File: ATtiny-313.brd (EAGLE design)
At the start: 27.6 x 64.1 mm, 14 parts

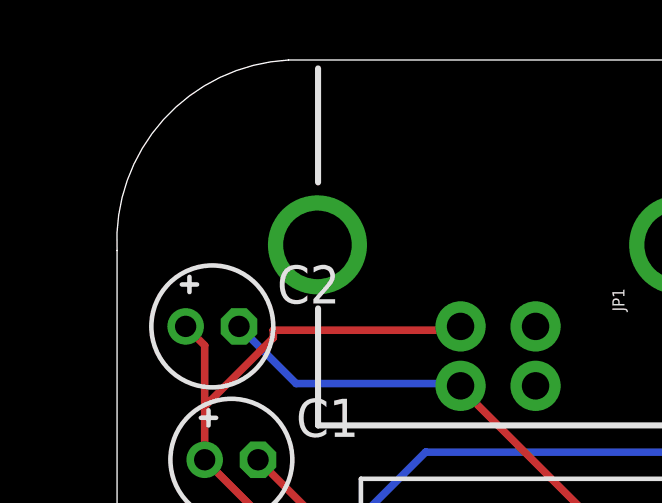
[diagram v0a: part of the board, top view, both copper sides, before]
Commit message: added link and OSHW logo
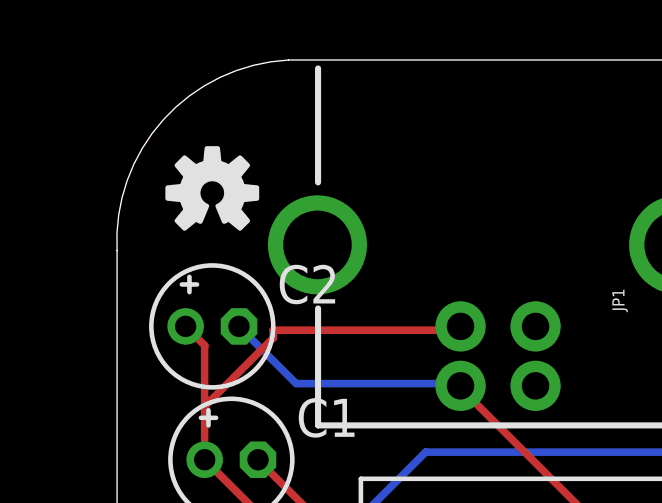
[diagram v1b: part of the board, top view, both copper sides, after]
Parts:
- added U$3: (no value), SparkFun-Aesthetics:OSHW-LOGO-S
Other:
- board text added: "http://github.com/jwhitehorn/ATtiny-313"
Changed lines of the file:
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@@
 <grid distance="0.025" unitdist="inch" unit="inch" style="lines" multiple="1" display="yes" altdistance="0.025" altunitdist="inch" altunit="inch"/>
 <layers>
-<layer number="1" name="Top" color="4" fill="1" visible="yes" active="yes"/>
+<layer number="1" name="Top" color="4" fill="1" visible="no" active="yes"/>
 <layer number="16" name="Bottom" color="1" fill="1" visible="yes" active="yes"/>
 <layer number="17" name="Pads" color="2" fill="1" visible="yes" active="yes"/>
@@
 <text x="32.385" y="36.83" size="1.016" layer="21">PD5</text>
 <text x="32.385" y="34.29" size="1.016" layer="21">GND</text>
+<text x="34.925" y="49.53" size="1.27" layer="22" rot="MR270">http://github.com/jwhitehorn/ATtiny-313</text>
 </plain>
 <attributes>
@@
 <element name="JP4" library="pinhead" package="1X01" value="" x="37.465" y="60.325"/>
 <element name="U$2" library="SparkFun-Electromechanical" package="STAND-OFF" value="" x="36.195" y="67.945"/>
+<element name="U$3" library="SparkFun-Aesthetics" package="OSHW-LOGO-S" value="" x="15.24" y="67.31"/>
 </elements>
 <signals>

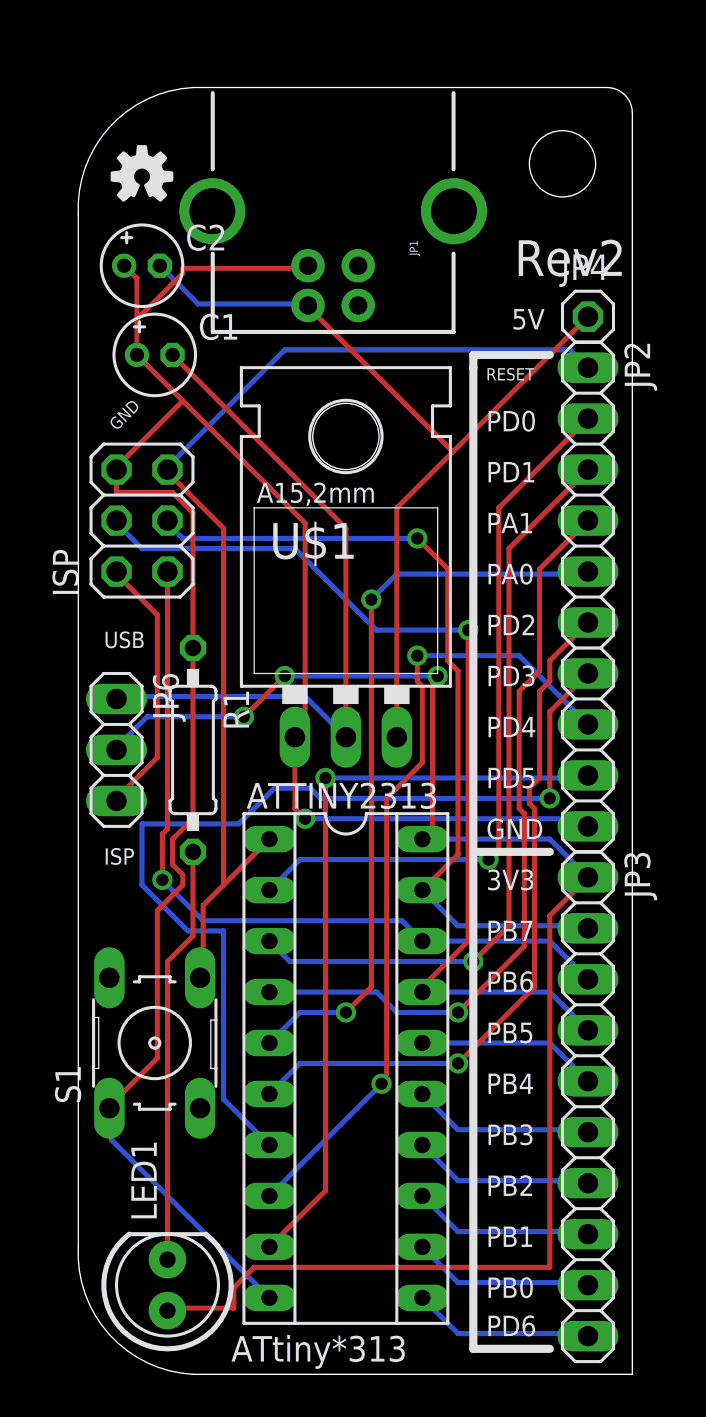
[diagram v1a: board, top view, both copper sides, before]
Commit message: use SMD to tighten up design
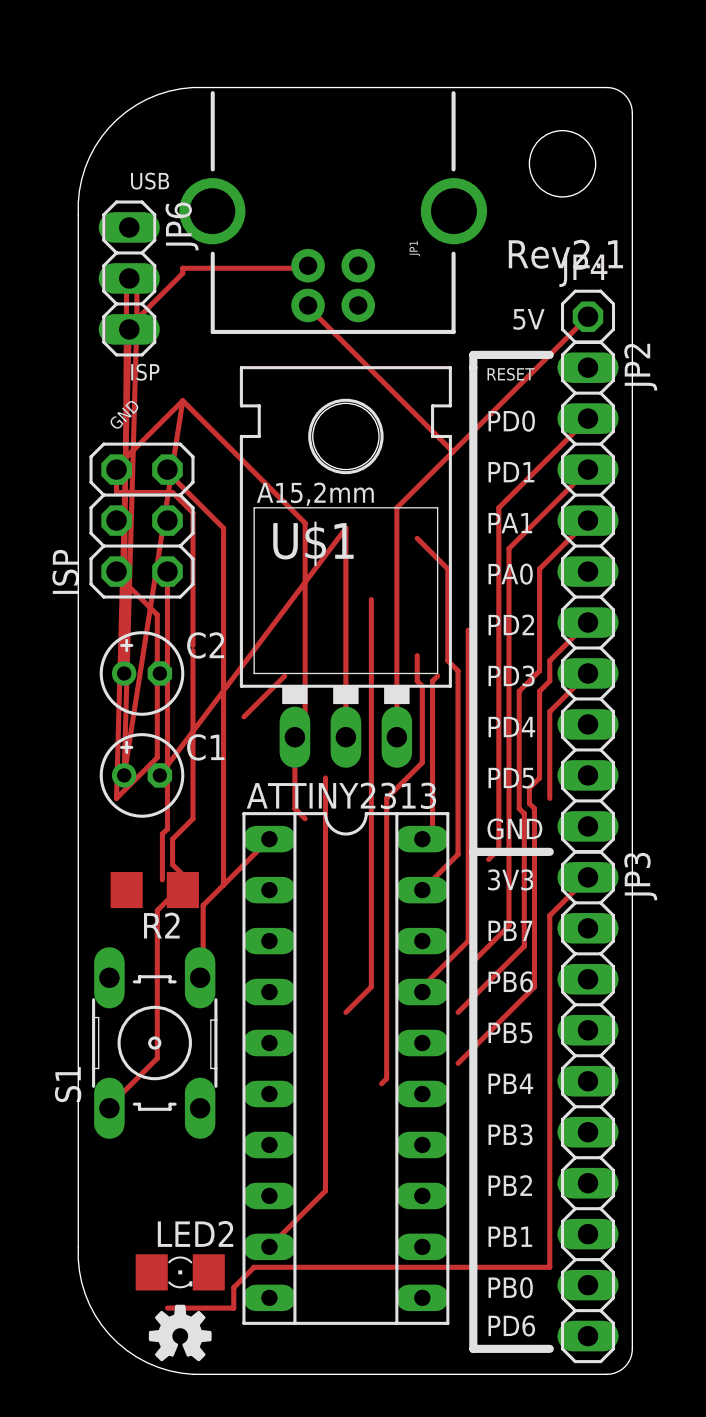
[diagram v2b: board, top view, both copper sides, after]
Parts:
- removed LED1: (no value), SparkFun-LED:LED5MM
- removed R1: 68, resistor:0207/10
- added LED2: (no value), led:1206
- added R2: 680, resistor:R3216
- moved U$3 57.8 mm to (17.1, 9.53)
- moved JP6 23.5 mm to (14.6, 62.2)
- moved C1 21.0 mm to (15.2, 37.5)
- moved C2 20.3 mm to (15.2, 42.5)
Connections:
- net N$2: now also LED2.A; no longer LED1.A
- net N$24: now also LED2.C, R2.2; no longer LED1.K, R1.2
- net N$3: now also R2.1; no longer R1.1
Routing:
- net N$11: track 48.0 -> 7.01 mm, vias 1 -> 0
- net N$3: track 110.5 -> 139.8 mm, vias 1 -> 0
- net N$16: track 47.9 -> 19.0 mm, vias 1 -> 0
- net N$2: track 75.9 -> 52.0 mm, vias 3 -> 0
- net N$5: track 54.1 -> 30.2 mm
- net ISP: track 38.7 -> 15.5 mm, vias 1 -> 0
- net N$23: track 13.1 -> 36.4 mm
- net N$14: track 41.0 -> 19.1 mm, vias 1 -> 0
- net N$24: track 20.8 -> 0.00 mm
- net N$12: track 40.1 -> 22.3 mm, vias 2 -> 0
- net N$9: track 36.9 -> 21.1 mm, vias 2 -> 0
- net N$13: track 37.7 -> 24.5 mm, vias 1 -> 0
- net N$6: track 35.6 -> 24.0 mm, vias 1 -> 0
- net N$7: track 37.5 -> 26.9 mm, vias 1 -> 0
- net N$10: track 34.9 -> 24.9 mm, vias 1 -> 0
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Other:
- outline, holes or cut-outs redrawn
- board text added: "Rev2.1"
- board text removed: "Rev2"

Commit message: more SMD goodness
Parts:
- removed U$1: V_REG_LD1117VXX, SparkFun-PowerIC:78XXL
- added IC1: REG1117, burr-brown:SOT223
- moved LED2 27.4 mm to (19.1, 40.0), turned to 270 degrees
- moved S1 18.8 mm to (26.0, 40.0), turned to 180 degrees
- moved C2 17.6 mm to (24.1, 57.8)
- moved JP6 15.3 mm to (29.2, 57.8)
- moved R2 14.9 mm to (21.0, 45.7), turned to 0 degrees
- moved C1 13.6 mm to (21.6, 49.5)
- moved ISP 7.10 mm to (18.4, 56.5), turned to 270 degrees
- moved JP1 2.54 mm to (24.8, 65.4)
- moved U$2 1.91 mm to (36.2, 69.8)
- moved U$3 1.80 mm to (18.4, 10.8), turned to 90 degrees
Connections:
- net N$1: now also IC1.3; no longer U$1.OUT
- net N$3: now also IC1.1; no longer U$1.IN
- net N$4: now also IC1.2; no longer U$1.GND
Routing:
- net N$4: track 25.8 -> 2.93 mm
- net N$5: track 30.2 -> 47.0 mm
- net N$23: track 36.4 -> 50.0 mm
- net ISP: track 15.5 -> 26.9 mm
- net N$1: track 35.2 -> 26.2 mm
- net N$3: track 139.8 -> 139.1 mm
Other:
- board size 27.6 x 64.1 mm -> 24.4 x 66 mm

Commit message: routing
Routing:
- net N$3: track 139.1 -> 88.8 mm, vias 0 -> 3
- net N$14: track 19.1 -> 66.7 mm, vias 0 -> 1
- net N$23: track 50.0 -> 11.5 mm, vias 0 -> 1
- net N$4: track 2.93 -> 39.7 mm, vias 0 -> 1
- net ISP: track 26.9 -> 63.2 mm, vias 0 -> 1
- net N$11: track 7.01 -> 32.2 mm, vias 0 -> 1
- net N$16: track 19.0 -> 42.8 mm
- net N$6: track 24.0 -> 46.7 mm, vias 0 -> 1
- net N$9: track 21.1 -> 36.3 mm, vias 0 -> 1
- net N$10: track 24.9 -> 38.5 mm, vias 0 -> 1
- net N$12: track 22.3 -> 32.9 mm, vias 0 -> 1
- net N$7: track 26.9 -> 37.2 mm, vias 0 -> 2
- net N$1: track 26.2 -> 35.8 mm
- net N$13: track 24.5 -> 34.1 mm, vias 0 -> 1
- net N$18: track 0.00 -> 9.04 mm
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
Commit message: tightened up the design
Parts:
- removed JP6: (no value), pinhead:1X03
- moved C1 38.3 mm to (17.8, 11.4)
- moved LED2 17.2 mm to (18.4, 22.9)
- moved C2 14.1 mm to (19.7, 44.5)
- moved U$3 8.64 mm to (25.4, 15.9), turned to 0 degrees
- moved JP1 7.65 mm to (24.1, 57.8)
- moved R2 7.24 mm to (19.1, 38.7), turned to 90 degrees
- moved U$2 6.63 mm to (34.3, 63.5)
- moved ISP 6.48 mm to (19.7, 50.2), turned to 180 degrees
- moved IC1 0.64 mm to (27.9, 48.9)
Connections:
- net ISP renamed MISO'
- net N$1 renamed 5V
- net N$14 renamed SCLK'
- net N$16 renamed MOSI'
- net N$3 renamed GND
- net N$5 renamed REST'
- removed net N$2: ATTINY2313.20, JP3.1, JP6.2, LED2.A
- removed net N$23: ISP.2, JP6.3
- removed net N$4: C1.-, IC1.2, JP6.1
- new net 3.3V: ATTINY2313.20, C1.-, IC1.2, JP3.1, LED2.A
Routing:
- net 3.3V: track 0.00 -> 70.7 mm
- net N$2: track 47.4 -> 0.00 mm, vias 2 -> 0
- net N$4: track 39.7 -> 0.00 mm, vias 1 -> 0
- net GND: track 88.8 -> 109.8 mm, vias 3 -> 1
- net SCLK': track 66.7 -> 49.0 mm
- net 5V: track 35.8 -> 47.9 mm
- net N$24: track 8.51 -> 20.1 mm
- net N$23: track 11.5 -> 0.00 mm, vias 1 -> 0
- net N$9: track 36.3 -> 47.4 mm, vias 1 -> 2
- net N$8: track 36.2 -> 46.1 mm, vias 1 -> 0
- net N$6: track 46.7 -> 37.3 mm
- net N$13: track 34.1 -> 41.5 mm, vias 1 -> 2
- net MISO': track 63.2 -> 57.0 mm, vias 1 -> 2
- net N$10: track 38.5 -> 34.5 mm, vias 1 -> 0
- net MOSI': track 42.8 -> 46.4 mm, vias 0 -> 1
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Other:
- board size 24.4 x 66 mm -> 24.4 x 59 mm
- board text added: "<"
- board text added: "Rev2.5"
- board text removed: "ISP"
- board text removed: "Rev2.1"
- board text removed: "USB"

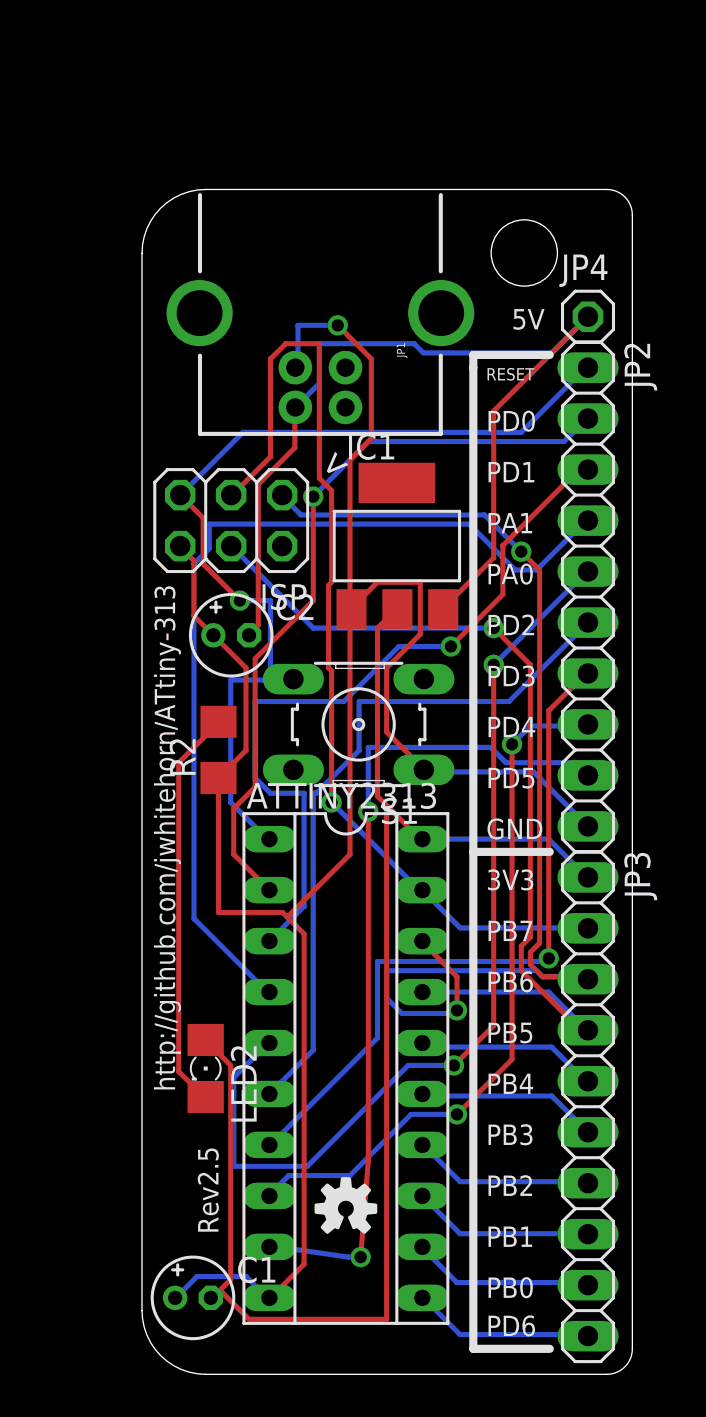
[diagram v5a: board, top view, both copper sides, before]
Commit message: added built in ISP
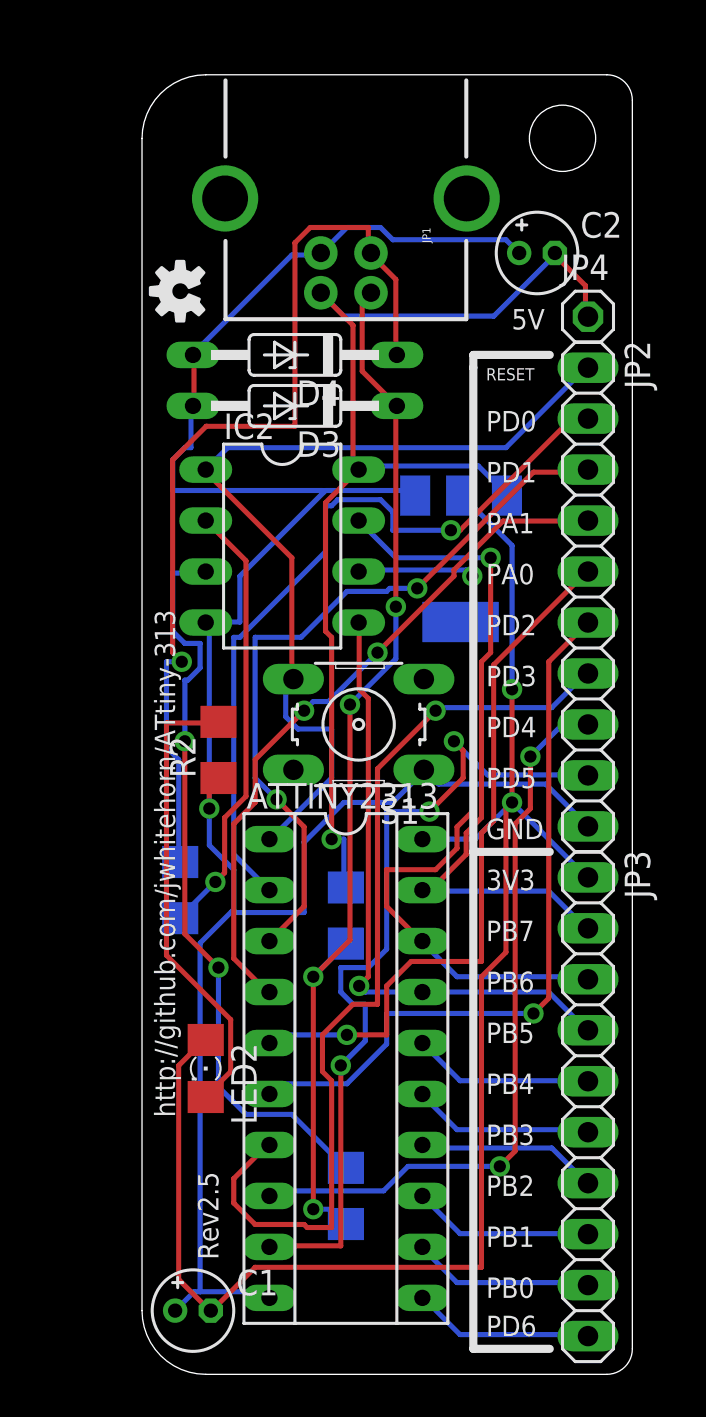
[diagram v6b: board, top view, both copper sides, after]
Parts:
- removed ISP: (no value), pinhead:2X03
- added D3, D4: 3.6V, .5W, diode:DO35Z10
- added IC2: ATtiny85, ic-package:DIL08
- added R1, R3: 68, resistor:R3216
- added R4: 1.5K, resistor:R3216
- moved U$3 46.5 mm to (17.1, 61.6), turned to 90 degrees
- moved C2 24.4 mm to (34.9, 63.5)
- moved U$2 6.02 mm to (36.2, 69.2)
- moved JP1 5.85 mm to (25.4, 63.5)
- moved IC1 3.24 mm to (31.1, 48.3), flipped to the bottom, turned to 180 degrees
- moved C1 0.63 mm to (17.8, 10.8)
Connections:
- new net D+': D4.C, JP1.D+, R1.2
- new net D-': D3.C, JP1.D-, R3.2, R4.1
- new net N$1: IC2.2, R1.1
- new net N$2: IC2.3, R3.1
- net 5V: now also IC2.8, R4.2
- net GND: now also D3.A, D4.A, IC2.4; no longer ISP.6
- net MISO': now also IC2.6; no longer ISP.1
- net MOSI': now also IC2.5; no longer ISP.4
- net REST': now also IC2.1; no longer ISP.5
- net SCLK': now also IC2.7; no longer ISP.3
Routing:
- net D-': track 0.00 -> 52.5 mm, vias 0 -> 4
- net D+': track 0.00 -> 48.1 mm, vias 0 -> 1
- net N$2: track 0.00 -> 37.4 mm, vias 0 -> 2
- net N$1: track 0.00 -> 22.0 mm, vias 0 -> 1
- net MISO': track 57.0 -> 37.0 mm, vias 2 -> 1
- net MOSI': track 46.4 -> 30.8 mm
- net SCLK': track 49.0 -> 34.6 mm
- net N$9: track 47.4 -> 35.3 mm, vias 2 -> 1
- net N$8: track 46.1 -> 34.5 mm, vias 0 -> 2
- net N$11: track 35.1 -> 46.4 mm
- net 5V: track 47.9 -> 57.7 mm, vias 0 -> 1
- net 3.3V: track 70.7 -> 79.9 mm, vias 0 -> 2
- net GND: track 109.8 -> 114.9 mm
- net REST': track 48.0 -> 44.9 mm, vias 1 -> 0
- net N$24: track 20.1 -> 23.1 mm
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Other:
- board size 24.4 x 59 mm -> 24.4 x 64.8 mm
- board text removed: "<"

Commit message: run ISP off 3.3v
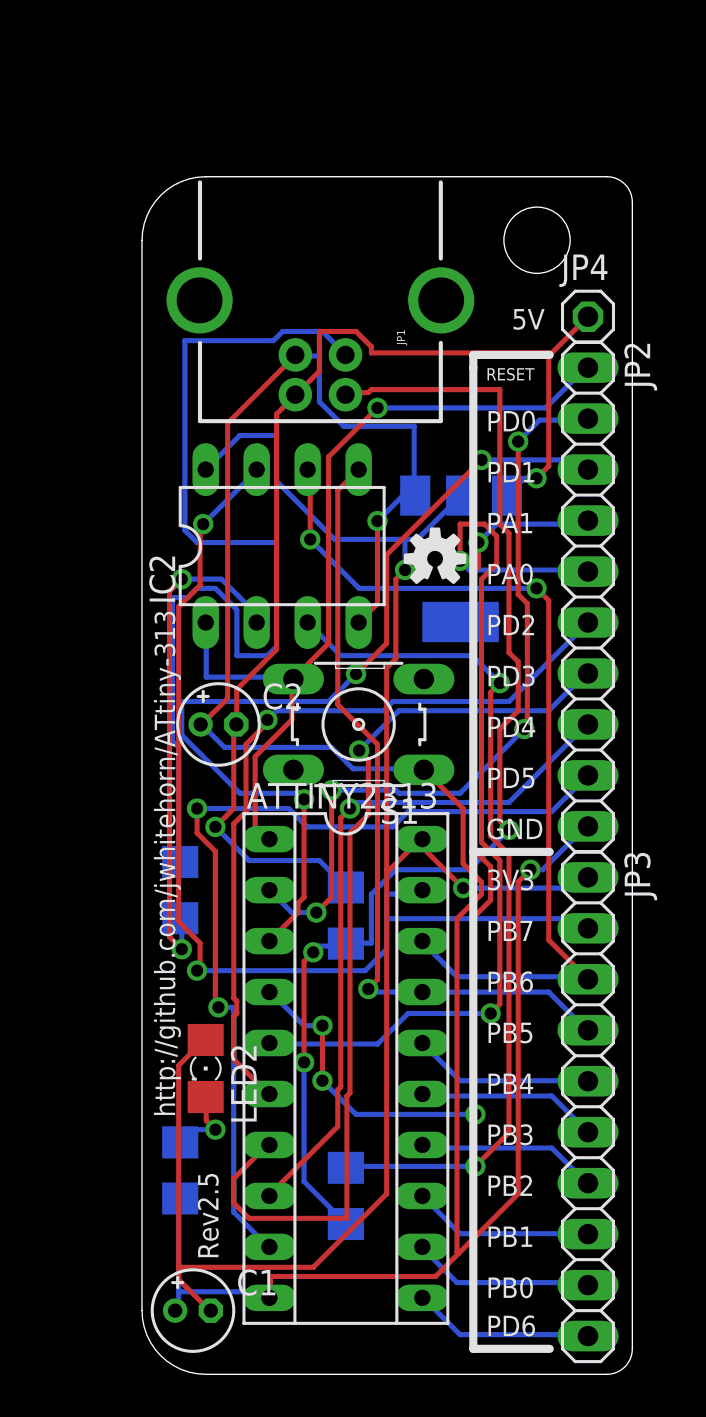
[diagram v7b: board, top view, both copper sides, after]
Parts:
- removed D3, D4: 3.6V, .5W, diode:DO35Z10
- moved C2 28.4 mm to (19.1, 40.0)
- moved R2 21.0 mm to (17.1, 17.8), flipped to the bottom
- moved U$3 18.4 mm to (29.8, 48.3), turned to 0 degrees
- moved U$2 5.24 mm to (34.9, 64.1)
- moved JP1 5.24 mm to (24.1, 58.4)
- turned IC2 to 0 degrees
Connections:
- net 3.3V: now also IC2.8
- net 5V: no longer IC2.8
- net D+': no longer D4.C
- net D-': no longer D3.C
- net GND: no longer D3.A, D4.A
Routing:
- net N$24: track 23.1 -> 3.83 mm, vias 0 -> 1
- net SCLK': track 34.6 -> 51.8 mm, vias 1 -> 2
- net N$8: track 34.5 -> 49.7 mm, vias 2 -> 4
- net N$9: track 35.3 -> 46.8 mm, vias 1 -> 2
- net 3.3V: track 79.9 -> 89.7 mm
- net GND: track 114.9 -> 124.4 mm, vias 1 -> 2
- net MISO': track 37.0 -> 45.4 mm, vias 1 -> 2
- net MOSI': track 30.8 -> 39.1 mm
- net N$7: track 36.9 -> 44.9 mm, vias 2 -> 3
- net D-': track 52.5 -> 59.0 mm, vias 4 -> 3
- net N$2: track 37.4 -> 42.7 mm
- net N$1: track 22.0 -> 25.4 mm, vias 1 -> 2
- net N$13: track 42.2 -> 44.7 mm, vias 3 -> 2
- net REST': track 44.9 -> 42.8 mm, vias 0 -> 1
- net N$12: track 36.7 -> 34.5 mm, vias 2 -> 1
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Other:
- board size 24.4 x 64.8 mm -> 24.4 x 59.7 mm

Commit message: work on rev 3
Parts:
- removed JP1: USB-B, SparkFun-Connectors:USB-B-PTH
- removed U$2: (no value), SparkFun-Electromechanical:STAND-OFF
- added JP5: (no value), pinhead:1X02
- added U$1: USB-MINIB-5PIN, SparkFun-Connectors:USB-MINIB
- moved C1 46.2 mm to (24.4, 56.5), turned to 180 degrees
- moved C2 19.1 mm to (29.1, 56.3), turned to 180 degrees
- moved R4 18.7 mm to (23.1, 49.0), turned to 0 degrees
- moved R3 17.1 mm to (19.1, 32.4), flipped to the top
- moved R1 12.8 mm to (19.1, 19.1), flipped to the top, turned to 270 degrees
- moved LED2 9.92 mm to (26.0, 16.5)
- moved R2 8.47 mm to (19.1, 26.0), flipped to the top
- moved S1 0.90 mm to (26.7, 39.4)
- moved ATTINY2313 0.64 mm to (26.0, 22.9)
- moved IC2 0.63 mm to (22.9, 48.9)
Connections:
- new net N$3: C1.-, IC1.2, JP5.1
- net 3.3V: now also JP5.2, R4.2; no longer C1.-, IC1.2
- net 5V: now also U$1.VBUS; no longer JP1.VBUS, R4.2
- net D+': no longer JP1.D+
- net D-': no longer JP1.D-
- net GND: now also U$1.GND; no longer JP1.GND
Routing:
- net D+': track 49.8 -> 0.00 mm
- net D-': track 59.0 -> 21.3 mm, vias 3 -> 1
- net 5V: track 57.7 -> 21.0 mm, vias 2 -> 0
- net N$2: track 42.7 -> 20.4 mm, vias 2 -> 0
- net 3.3V: track 89.7 -> 69.2 mm, vias 2 -> 1
- net N$8: track 49.7 -> 32.8 mm, vias 4 -> 1
- net N$9: track 46.8 -> 32.5 mm, vias 2 -> 1
- net N$3: track 0.00 -> 13.7 mm
- net N$24: track 3.83 -> 17.2 mm, vias 1 -> 0
- net N$11: track 46.6 -> 33.9 mm
- net N$7: track 44.9 -> 33.1 mm, vias 3 -> 1
- net GND: track 124.4 -> 112.8 mm, vias 2 -> 0
- net N$13: track 44.7 -> 33.9 mm, vias 2 -> 1
- net N$6: track 38.7 -> 30.6 mm, vias 4 -> 1
- net MISO': track 45.4 -> 38.8 mm, vias 2 -> 0
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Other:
- board size 24.4 x 59.7 mm -> 22.5 x 61.3 mm
- board text added: "POWER"
- board text added: "RST"
- board text added: "Rev3"
- board text removed: "Rev2.5"
- board text removed: "http://github.com/jwhitehorn/ATtiny-313"
